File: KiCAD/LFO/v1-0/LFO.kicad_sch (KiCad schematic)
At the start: 13 parts, among them J1 OUT, J2 OUT, J3 Conn_01x03, J4 Conn_01x03, SW1 SW_SPDT, U1 TL072

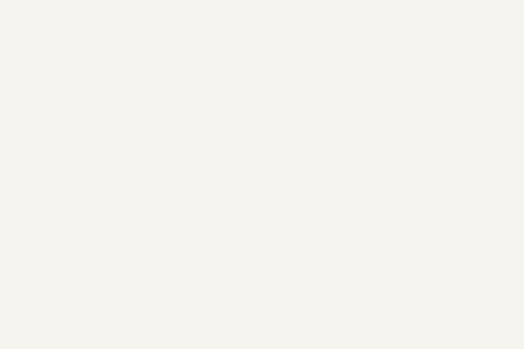
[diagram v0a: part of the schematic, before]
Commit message: Footprint Edits
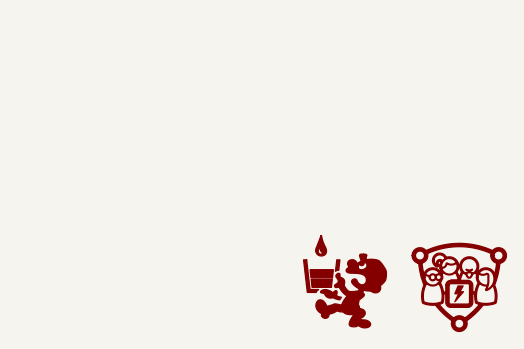
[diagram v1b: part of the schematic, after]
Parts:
- added G1: ~, symbol HackSynth:CCHS_Logo
- added G2: ~, symbol HackSynth:Logo_PancakeLegend
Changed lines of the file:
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@@
+	)
+	(symbol
+		(lib_id "HackSynth:CCHS_Logo")
+		(at 275.59 172.72 0)
+		(unit 1)
+		(exclude_from_sim no)
+		(in_bom yes)
+		(on_board yes)
+		(dnp no)
+		(fields_autoplaced yes)
+		(property "Reference" "G1"
+			(at 275.59 180.34 0)
+			(effects
+				(font
+					(size 1.27 1.27)
+				)
+				(hide yes)
+			)
+		)
+		(property "Value" "~"
+			(at 281.94 173.89 0)
+			(effects
+				(font
+					(size 1.27 1.27)
+				)
+				(justify left)
+			)
+		)
+		(property "Footprint" ""
+			(at 275.59 172.72 0)
+			(effects
+				(font
+					(size 1.27 1.27)
+				)
+				(hide yes)
+			)
+		)
+		(property "Datasheet" ""
+			(at 275.59 172.72 0)
+			(effects
+				(font
+					(size 1.27 1.27)
+				)
+				(hide yes)
+			)
+		)
+		(property "Description" ""
+			(at 275.59 172.72 0)
+			(effects
+				(font
+					(size 1.27 1.27)
+				)
+				(hide yes)
+			)
+		)
+		(instances
+			(project "LFO"
+				(path "/cf31493f-2592-4a10-a419-2df89491bd24"
+					(reference "G1")
+					(unit 1)
+				)
+			)
+		)
 	)
 	(symbol
@@
 				)
 			)
+		)
+	)
+	(symbol
+		(lib_id "HackSynth:Logo_PancakeLegend")
+		(at 262.89 173.355 0)
+		(unit 1)
+		(exclude_from_sim no)
+		(in_bom yes)
+		(on_board yes)
+		(dnp no)
+		(fields_autoplaced yes)
+		(property "Reference" "G2"
+			(at 262.89 180.975 0)
+			(effects
+				(font
+					(size 1.27 1.27)
+				)
+				(hide yes)
+			)
+		)
+		(property "Value" "~"
+			(at 269.24 173.2549 0)
+			(effects
+				(font
+					(size 1.27 1.27)
+				)
+				(justify left)
+			)
+		)
+		(property "Footprint" ""
+			(at 262.89 173.355 0)
+			(effects
+				(font
+					(size 1.27 1.27)
+				)
+				(hide yes)
+			)
+		)
+		(property "Datasheet" ""
+			(at 262.89 173.355 0)
+			(effects
+				(font
+					(size 1.27 1.27)
+				)
+				(hide yes)
+			)
+		)
+		(property "Description" ""
+			(at 262.89 173.355 0)
+			(effects
+				(font
+					(size 1.27 1.27)
+				)
+				(hide yes)
+			)
+		)
+		(instances
+			(project "LFO"
+				(path "/cf31493f-2592-4a10-a419-2df89491bd24"
+					(reference "G2")
+					(unit 1)
+				)
+			)

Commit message: Fixes
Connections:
- net at RV1.1, RV1.2: now also R1.1; no longer R1.2, SW1.1 (A)
- net at C1.1, U1.2 (-): now also R1.2, SW1.1 (A); no longer R1.1
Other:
- moved on the sheet: R1
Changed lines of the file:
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@@
+	)
+	(junction
+		(at 49.53 93.98)
+		(diameter 0)
+		(color 0 0 0 0)
 	)
 	(junction
@@
 	)
 	(junction
-		(at 49.53 93.98)
-		(diameter 0)
-		(color 0 0 0 0)
-	)
-	(junction
 		(at 137.16 93.98)
 		(diameter 0)
@@
 	(wire
 		(pts
-			(xy 49.53 113.03) (xy 49.53 106.68)
-		)
-		(stroke
-			(width 0)
-			(type default)
-		)
-	)
-	(wire
-		(pts
 			(xy 124.46 113.03) (xy 124.46 105.41)
 		)
@@
 	(wire
 		(pts
-			(xy 49.53 93.98) (xy 69.85 93.98)
+			(xy 49.53 93.98) (xy 52.07 93.98)
 		)
 		(stroke
@@
 	(wire
 		(pts
-			(xy 49.53 93.98) (xy 49.53 99.06)
+			(xy 49.53 93.98) (xy 49.53 113.03)
 		)
 		(stroke
@@
 		(pts
 			(xy 139.7 88.9) (xy 134.62 88.9)
+		)
+		(stroke
+			(width 0)
+			(type default)
+		)
+	)
+	(wire
+		(pts
+			(xy 59.69 93.98) (xy 69.85 93.98)
 		)
 		(stroke
@@
 	(symbol
 		(lib_id "HackSynth:R")
-		(at 49.53 102.87 180)
+		(at 55.88 93.98 270)
 		(unit 1)
 		(exclude_from_sim no)
@@
 		(dnp no)
 		(property "Reference" "R1"
-			(at 47.498 101.854 0)
-			(effects
-				(font
-					(size 1.27 1.27)
-				)
-				(justify left)
+			(at 55.88 87.63 90)
+			(effects
+				(font
+					(size 1.27 1.27)
+				)
 			)
 		)
 		(property "Value" "10k"
-			(at 47.498 103.8861 0)
-			(effects
-				(font
-					(size 1.27 1.27)
-				)
-				(justify left)
+			(at 55.88 90.17 90)
+			(effects
+				(font
+					(size 1.27 1.27)
+				)
 			)
 		)
 		(property "Footprint" "HackSynth:R_Axial_DIN0207_L6.3mm_D2.5mm_P7.62mm_Horizontal"
-			(at 51.308 102.87 90)
+			(at 55.88 92.202 90)
 			(effects
 				(font
@@
 		)
 		(property "Datasheet" "~"
-			(at 49.53 102.87 0)
+			(at 55.88 93.98 0)
 			(effects
 				(font
@@
 		)
 		(property "Description" "Resistor"
-			(at 49.53 102.87 0)
-			(effects
-				(font
+			(at 55.88 93.98 0)
+			(effects
+				(font
